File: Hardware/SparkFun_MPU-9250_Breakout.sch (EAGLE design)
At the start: 18 parts, among them U1 MPU-9250

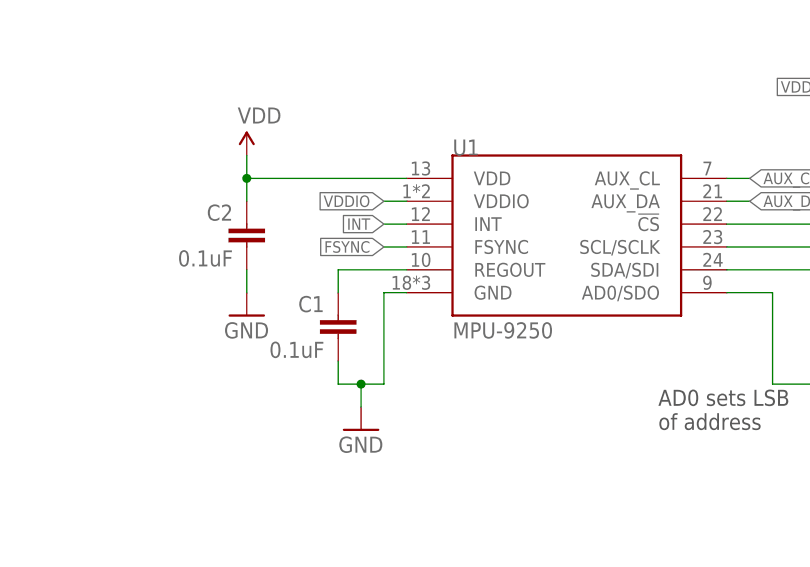
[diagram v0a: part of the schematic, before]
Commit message: Removed exposed pad copper from PCB
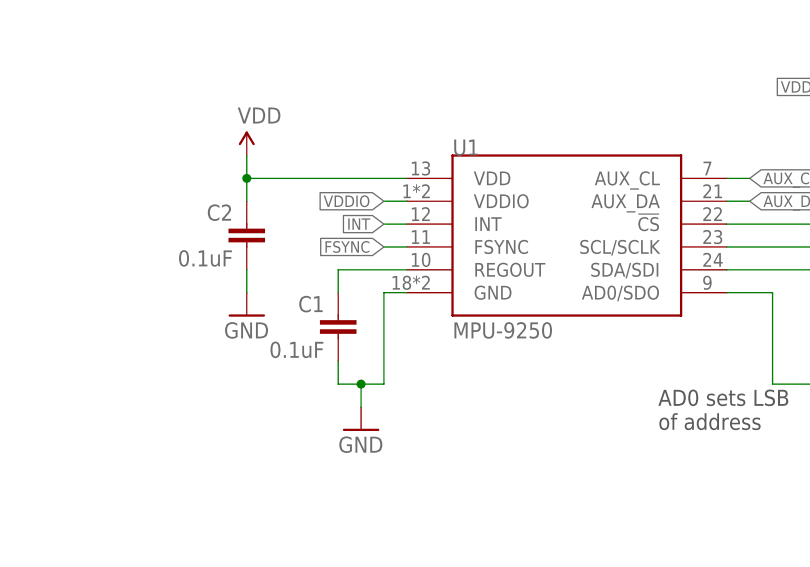
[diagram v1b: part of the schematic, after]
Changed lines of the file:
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@@
 <?xml version="1.0" encoding="utf-8"?>
 <!DOCTYPE eagle SYSTEM "eagle.dtd">
-<eagle version="7.5.0">
+<eagle version="7.6.0">
 <drawing>
 <settings>
